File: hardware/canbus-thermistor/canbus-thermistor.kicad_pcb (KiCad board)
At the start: 2 copper layers, 33 parts, among them J1 USB_B_Micro, J2 UART, J3 NTC Thermistor, J4 CANBus, J5 CANBus, J6 SWD, Q1 2N7002, Q2 2N7002, U1 MCP1754S-3302xCB, U2 STM32F042F6Px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

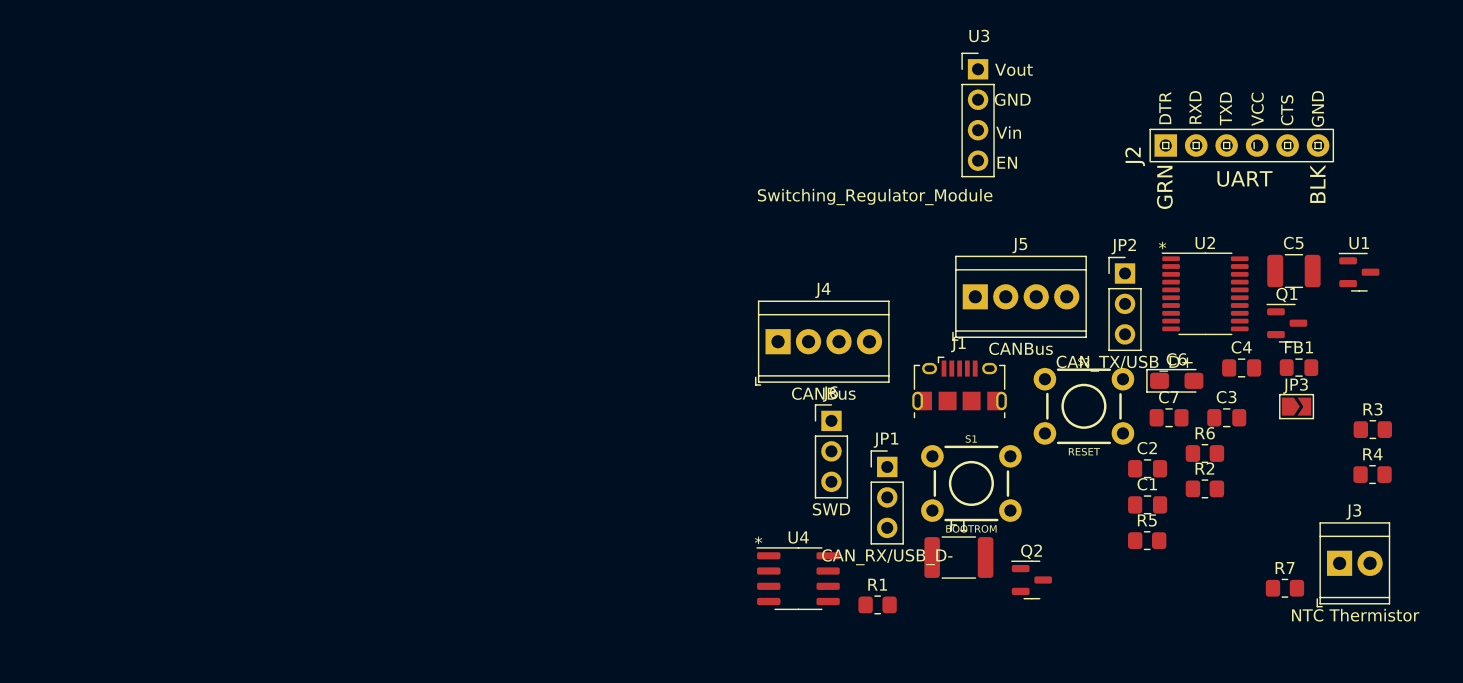
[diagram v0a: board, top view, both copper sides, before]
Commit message: Add CANBus Thermistor layout
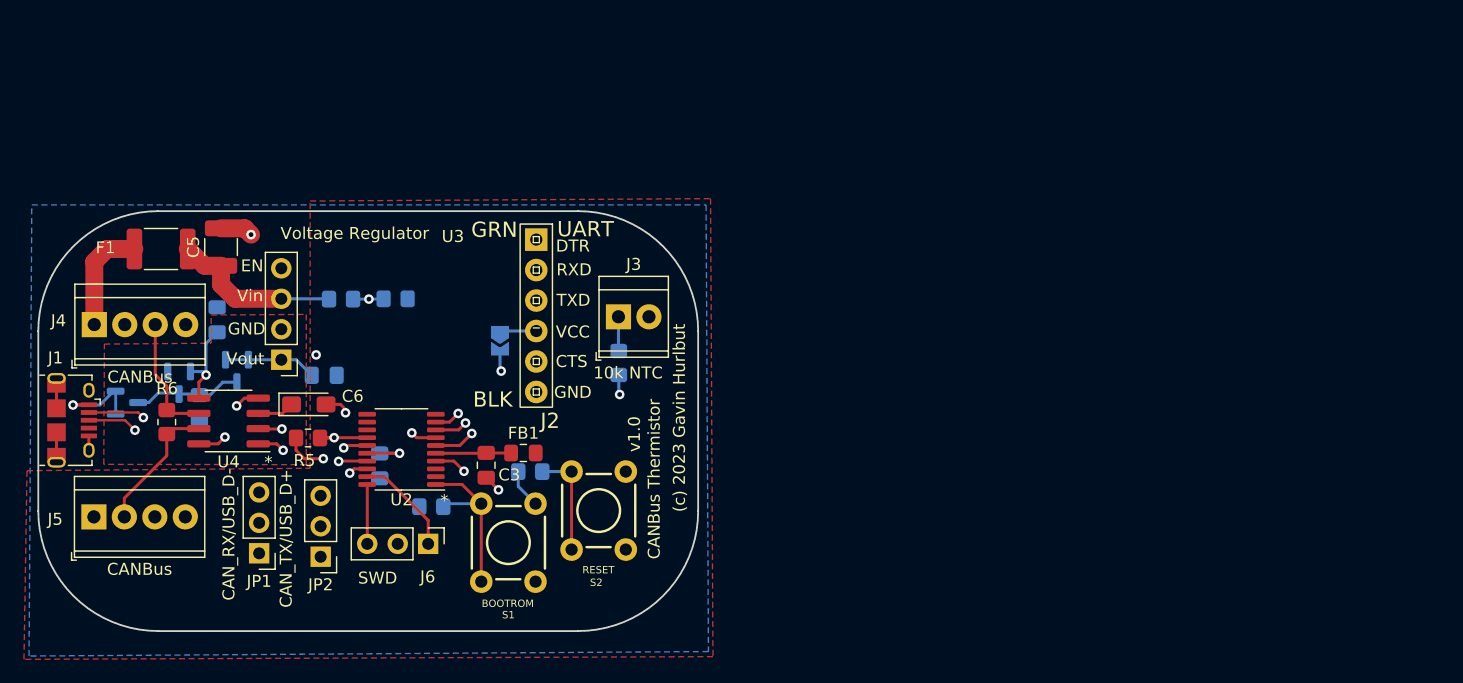
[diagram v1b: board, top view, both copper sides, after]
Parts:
- added BOARD: Altoid-Board-Outline, Beirdo:Altoid-Board-Outline, F.Cu at (55.0, 68.6)
- C1, C2, C4, C7, JP3, Q1, Q2, R1, R2, R3, R4, R7, U1: moved to B.Cu
- J3: value NTC Thermistor -> 10k NTC
- U3: value Switching_Regulator_Module -> Voltage Regulator
- moved U1 98.8 mm to (66.7, 82.9), turned to -90 degrees
- moved C5 89.4 mm to (70.2, 71.6), turned to 90 degrees
- moved Q1 87.6 mm to (71.5, 81.9), turned to -90 degrees
- moved R3 86.7 mm to (80.2, 76.0)
- moved R6 86.6 mm to (65.7, 86.2), turned to 90 degrees
- moved C4 85.5 mm to (69.9, 77.7), turned to 90 degrees
- moved R4 82.7 mm to (84.8, 75.9)
- moved C2 79.2 mm to (68.4, 85.0), turned to -90 degrees
- moved Q2 76.9 mm to (62.4, 84.6)
- moved J5 75.7 mm to (59.6, 94.1)
- moved J1 74.0 mm to (57.8, 86.0), turned to -90 degrees
- moved C6 72.4 mm to (77.5, 84.7)
- moved F1 71.3 mm to (65.2, 71.8)
- moved JP2 71.1 mm to (78.5, 97.4), turned to 180 degrees
- moved C7 70.5 mm to (78.8, 82.3)
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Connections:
- net Net-(C3-Pad1) renamed /VDDA
- C4 pad 1: Net-(C4-Pad1) -> +3V3
- S1 pad 2: (no net) -> unconnected-(S1-Pad2)
- S1 pad 4: (no net) -> unconnected-(S1-Pad4)
- S2 pad 2: (no net) -> unconnected-(S2-Pad2)
- S2 pad 4: (no net) -> unconnected-(S2-Pad4)
- U1 pad 2: Net-(C4-Pad1) -> +3V3
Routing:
- net CANH: track 0.00 -> 27.3 mm
- net +BATT: track 0.00 -> 26.4 mm
- net CANL: track 0.00 -> 26.4 mm
- net VTHERM: track 0.00 -> 25.1 mm, vias 0 -> 1
- net USB_D+: track 0.00 -> 22.8 mm, vias 0 -> 1
- net +3V3: track 0.00 -> 22.3 mm, vias 0 -> 6
- net ~{RESET}: track 0.00 -> 20.6 mm, vias 0 -> 1
- net VBAT_MON: track 0.00 -> 17.4 mm, vias 0 -> 2
- net CAN_STBY: track 0.00 -> 17.0 mm, vias 0 -> 2
- net USB_D-: track 0.00 -> 17.0 mm, vias 0 -> 1
- net RXD2: track 0.00 -> 16.8 mm, vias 0 -> 1
- net GND: track 0.00 -> 16.5 mm, vias 0 -> 5
- net TXD2: track 0.00 -> 15.4 mm, vias 0 -> 1
- net CAN_RX: track 0.00 -> 15.1 mm, vias 0 -> 1
- net +12V: track 0.00 -> 14.4 mm
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- added copper zone on F.Cu, net +3V3
- added copper zone on In2.Cu, net +3V3
- added copper zone on F.Cu, net +5V
- added copper zone on B.Cu, net GND
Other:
- board outline added: 55 x 35 mm
- copper layers 2 -> 4
- board text added: "(c) 2023 Gavin Hurlbut"
- board text added: "CANBus Thermistor"
- board text added: "v1.0"

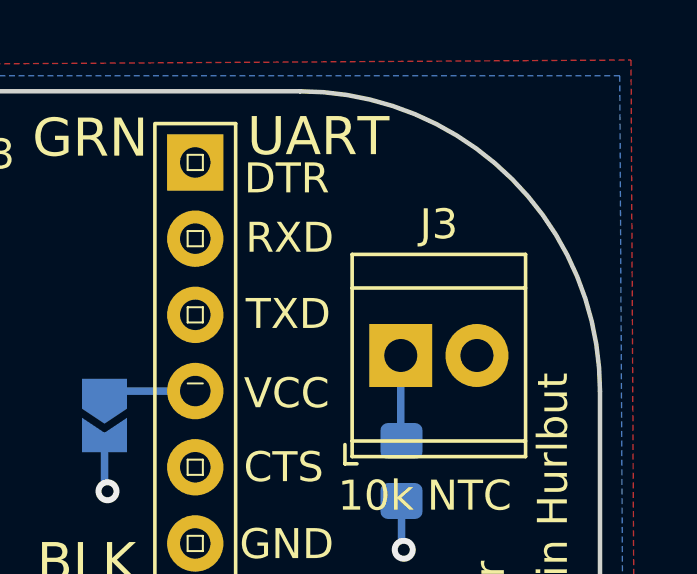
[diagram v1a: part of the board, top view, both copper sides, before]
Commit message: Updated the thermocouple board, added OSHW to bottom of all boards
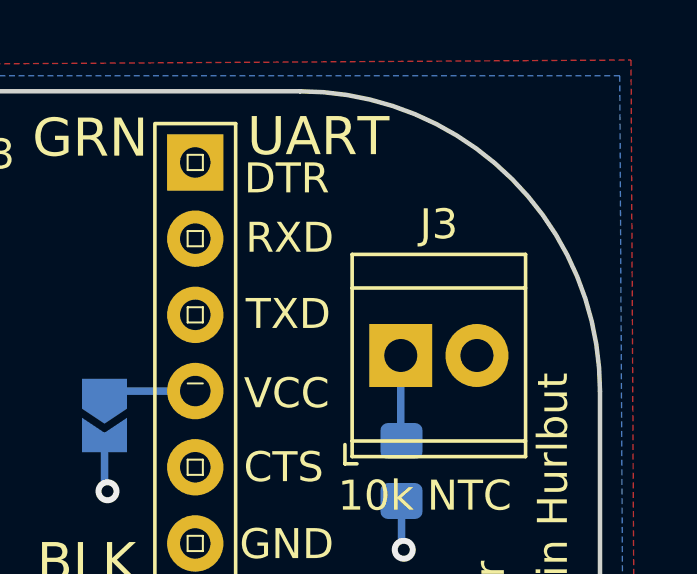
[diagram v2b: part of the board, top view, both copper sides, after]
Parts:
- added REF**: OSHW-Logo2_7.3x6mm_SilkScreen, Symbol:OSHW-Logo2_7.3x6mm_SilkScreen, B.Cu at (87.1, 80.6)
